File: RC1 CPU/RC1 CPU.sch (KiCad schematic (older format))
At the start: 43 parts, among them J1 Expansion, J2 RC1_UI_Port, J3 BARREL_JACK, M1 Mounting, M2 Mounting, M3 Mounting, M4 Mounting, U1 WD65C02, U2 HM62256BLP-7, U3 28C256, U4 6532, U5 74LS00, U6 LM556, U7 74LS145, U8 74LS138, U9 74LS00, X1 1MHz

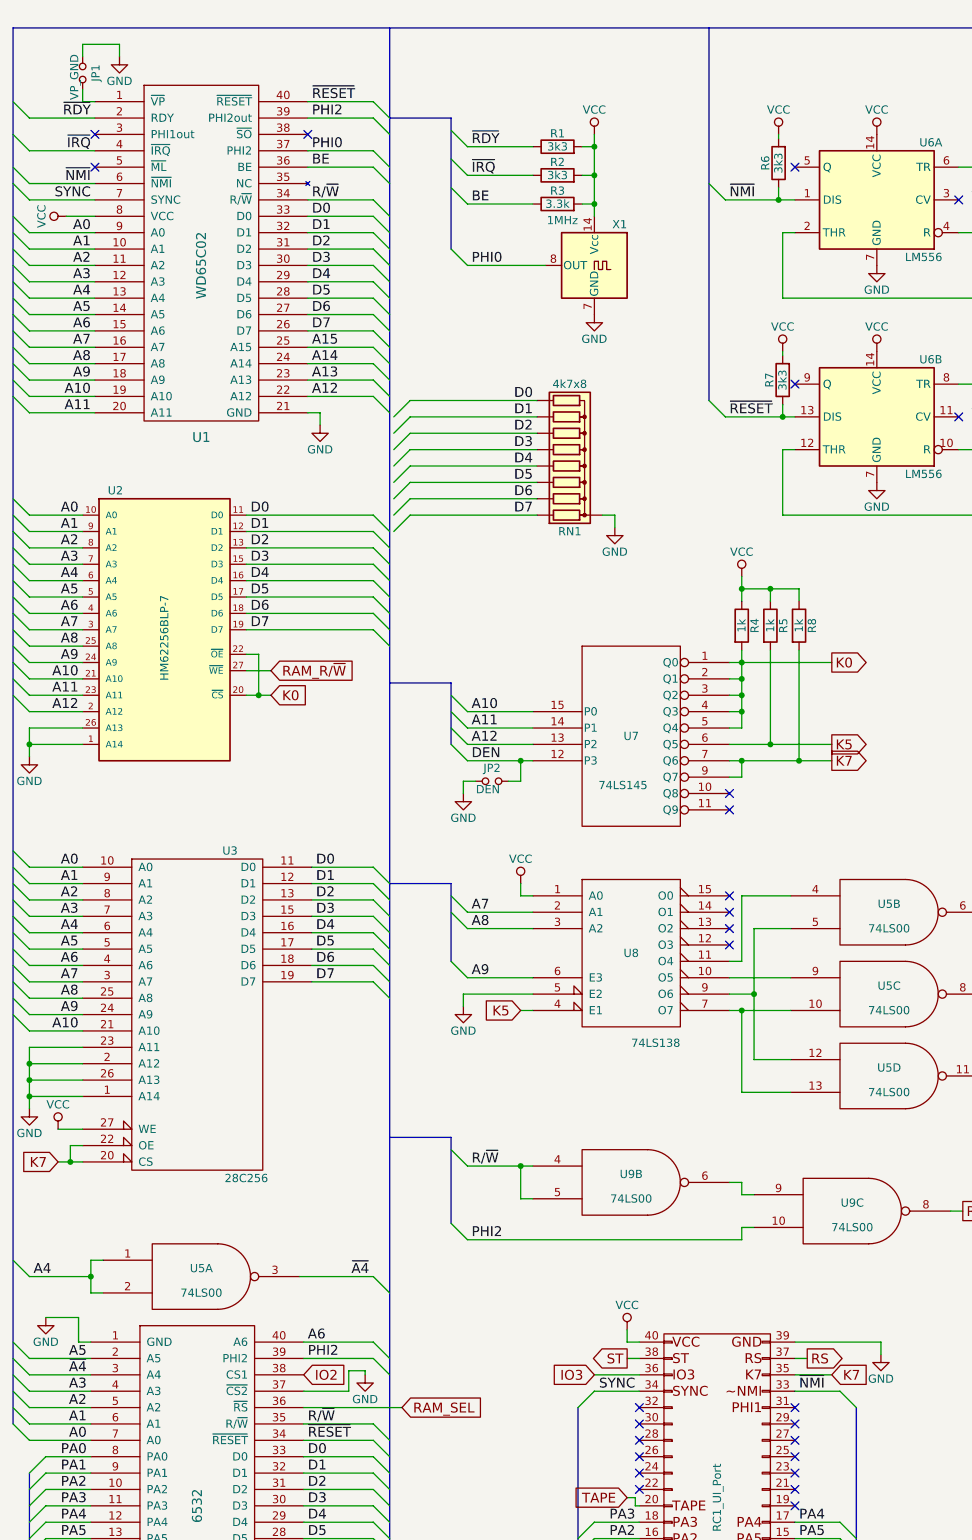
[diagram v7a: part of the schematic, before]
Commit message: Added phi1 to UI connector
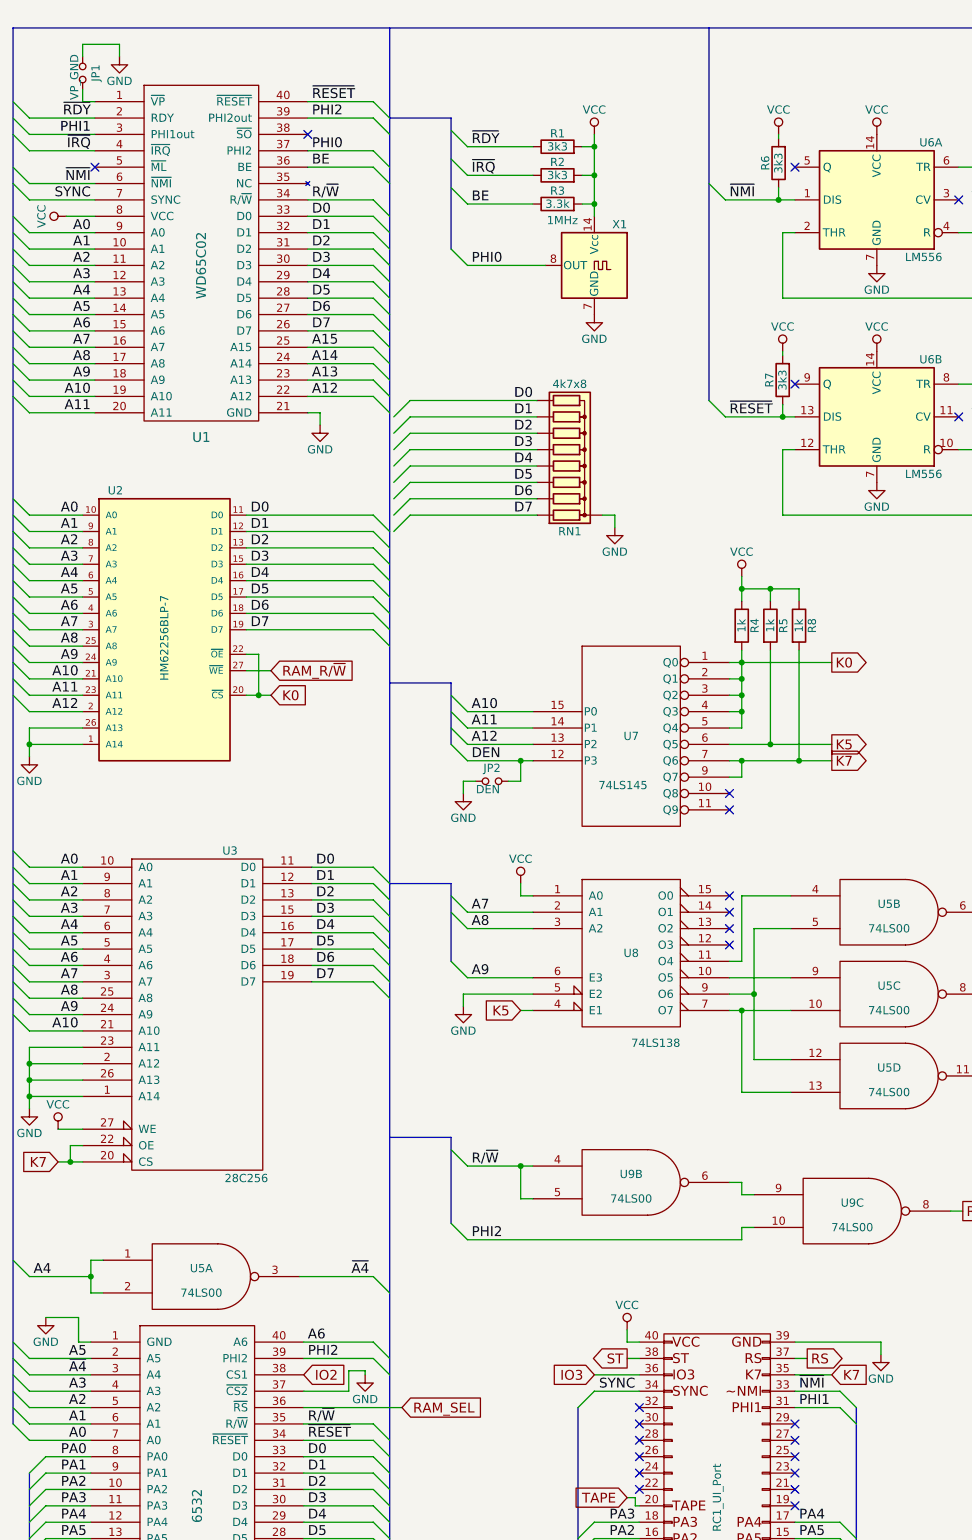
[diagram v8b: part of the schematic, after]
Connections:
- net PHI1: now reaches J2.31 (P31)
- net PHI1: now also U1.3 (PHI1out)
- no-connect marks 27 -> 25
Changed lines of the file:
@@
 Text Label 2700 2000 0    60   ~ 0
 R/~W
-NoConn ~ 1375 1600
 $Comp
 L GND #PWR010
@@
 NoConn ~ 5650 9575
 NoConn ~ 5650 9475
-NoConn ~ 5650 9375
 $Comp
 L 74LS00 U9
@@
 Wire Wire Line
 	4675 9975 4700 9975
+Entry Wire Line
+	875  1500 975  1600
+Wire Wire Line
+	975  1600 1375 1600
+Text Label 1350 1600 2    60   ~ 0
+PHI1
+Text Label 5675 9375 0    60   ~ 0
+PHI1
+Entry Wire Line
+	5925 9375 6025 9475
+Wire Wire Line
+	5925 9375 5650 9375
 $EndSCHEMATC
